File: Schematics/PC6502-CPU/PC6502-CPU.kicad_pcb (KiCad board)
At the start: 4 copper layers, 100 x 100 mm, 79 parts, among them J1 BUS, J2 Conn_01x02, J3 USB_C_Receptacle_USB2.0_16P, J4 TEST, J5 Conn_02x05_Odd_Even, J6 Conn_02x02_Odd_Even, Q1 IRLML6402, U2 AS6C4008-55PCN, U3 SST39SF010, U4 ATF1504AS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

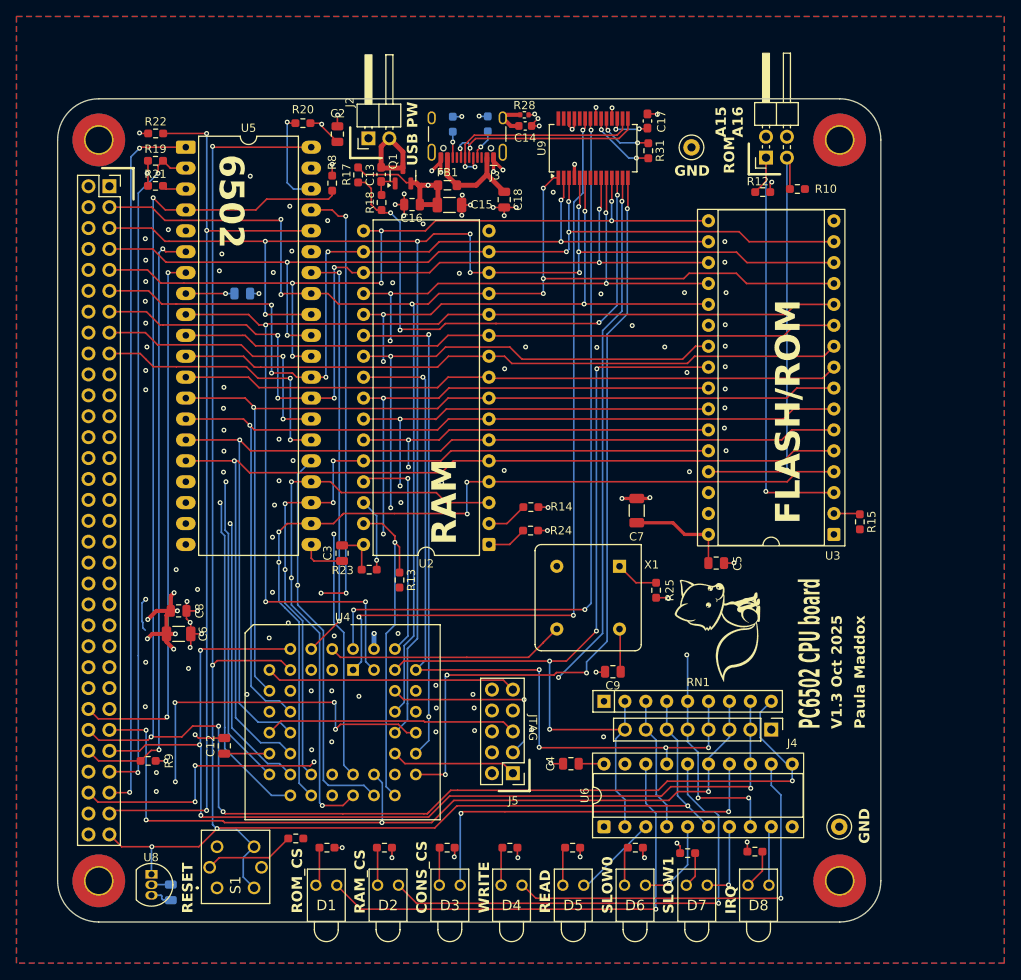
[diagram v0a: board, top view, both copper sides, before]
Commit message: Updated CPU to Rev 1.4
VErsion 1.4 of CPU board connects A15 direct to RAM and should allow me to get more than 32K of RAM available.
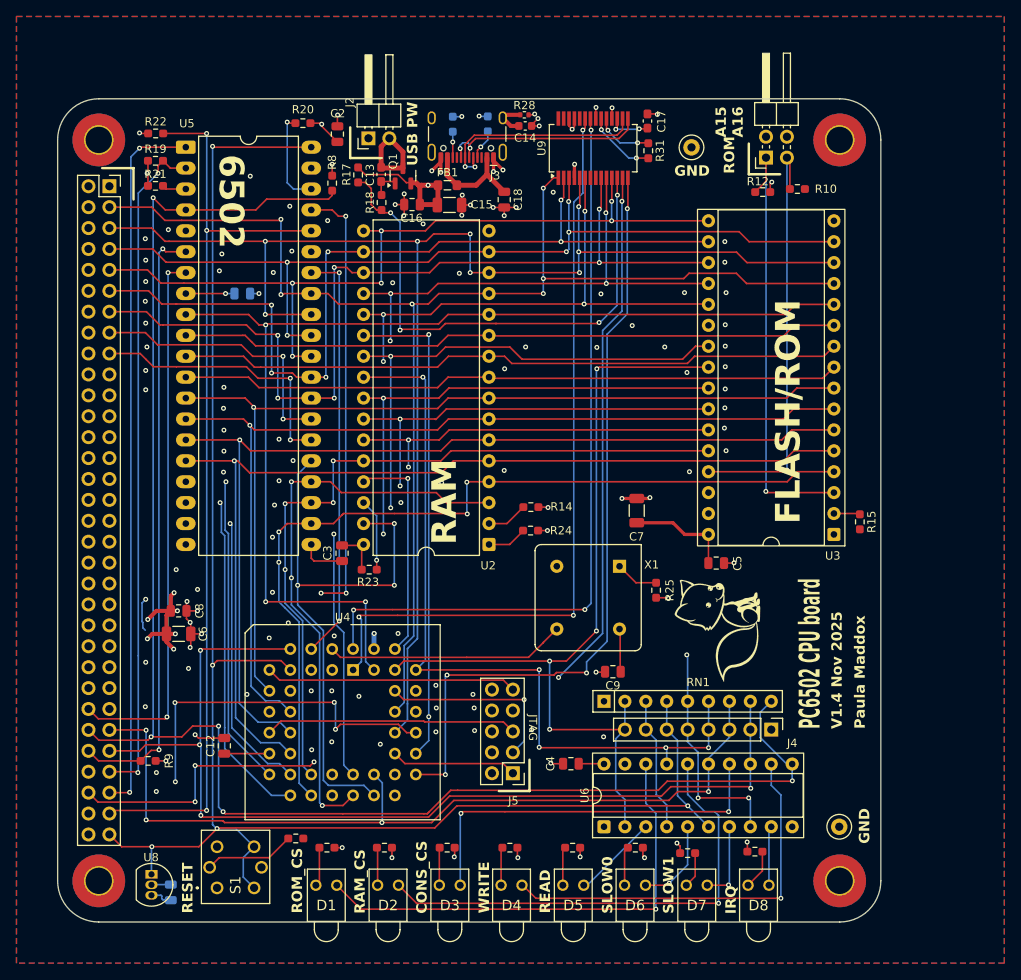
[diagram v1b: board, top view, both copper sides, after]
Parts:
- removed R13: 10K, Resistor_SMD:R_0603_1608Metric_Pad0.98x0.95mm_HandSolder
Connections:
- U2 pad 31: RAM_A15 -> /A15
- U4 pad 28: RAM_A15 -> unconnected-(U4-I/O-Pad28)
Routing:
- net RAM_A15: track 40.7 -> 0.00 mm, vias 1 -> 0
- net /A15: track 75.7 -> 98.7 mm, vias 1 -> 3
- net GND: vias 118 -> 119
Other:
- board text added: "V1.4 Nov 2025"
- board text removed: "V1.3 Oct 2025"
